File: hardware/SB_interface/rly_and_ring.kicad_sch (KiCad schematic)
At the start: 12 parts, among them K2 J104D2C12VDC.36S, Q3 2N7002

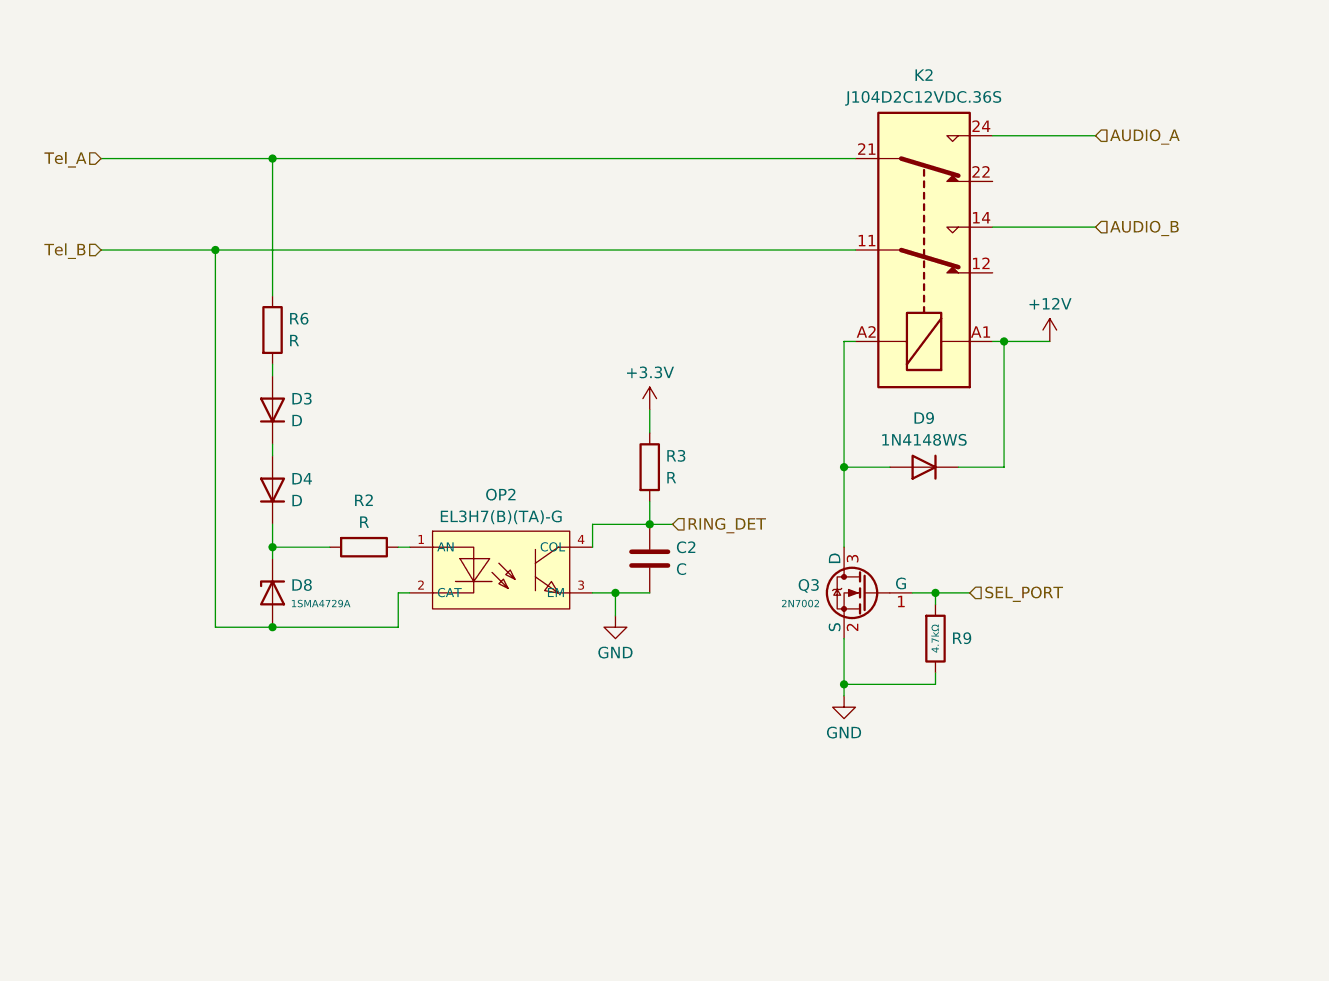
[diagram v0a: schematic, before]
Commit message: current source for ring det. + main 8p8c pinout corrected
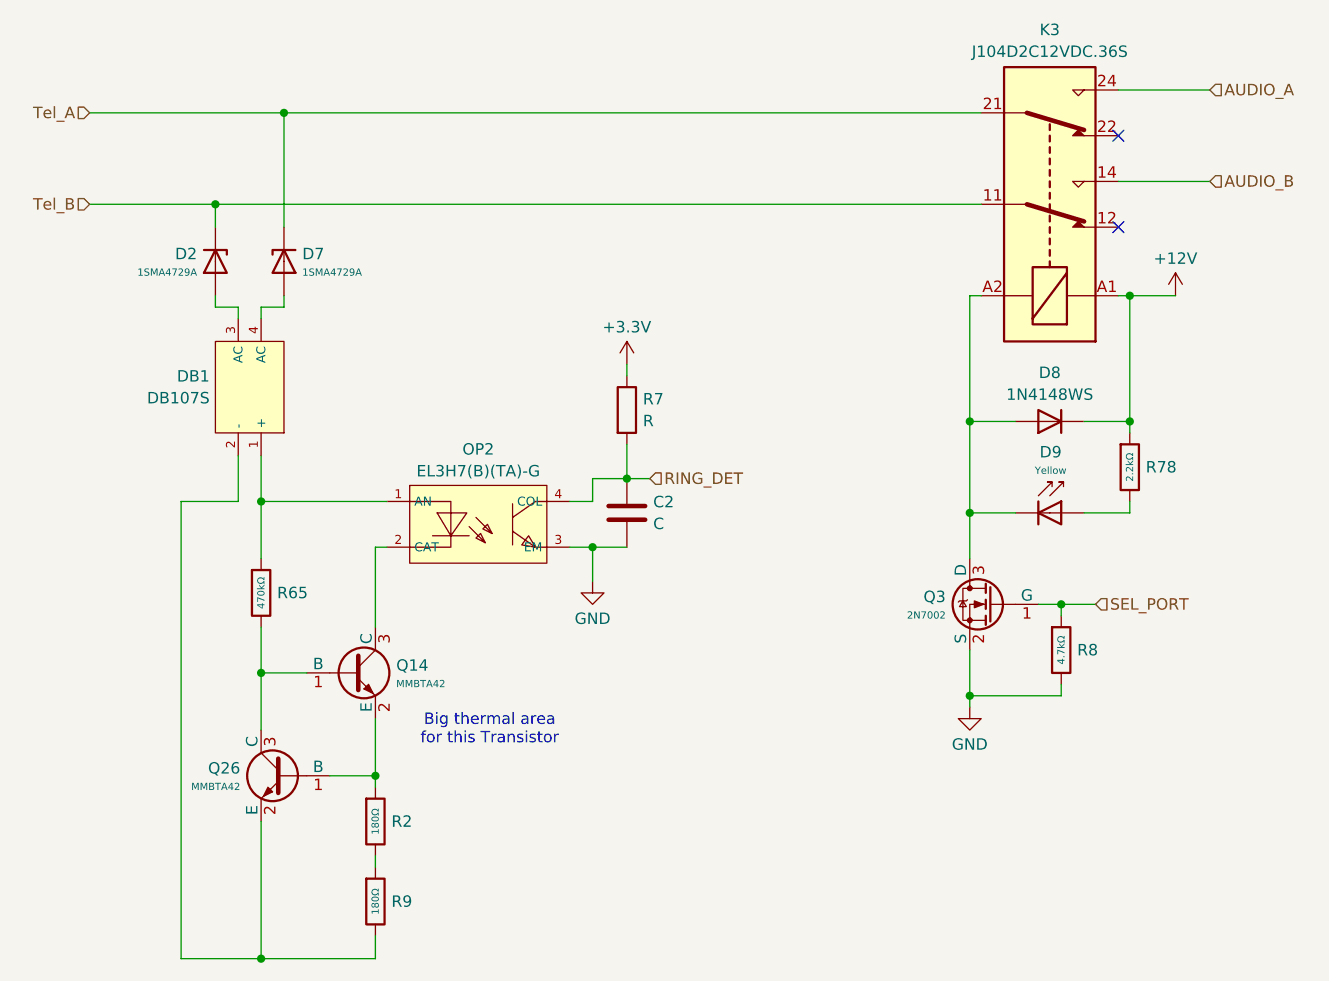
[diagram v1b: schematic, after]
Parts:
- removed D3, D4: D, symbol Device:D
- removed R2, R6: R, symbol Device:R
- added D2: 1SMA4729A, PCM_JLCPCB:D_SMA, symbol PCM_JLCPCB-Diodes:Zener,1SMA4729A
- added D9: Yellow, PCM_JLCPCB:D_0805, symbol PCM_JLCPCB-Diodes:LED,0805,Yellow
- added DB1: DB107S, PCM_JLCPCB:DBS_L8.2-W6.4-P5.10-LS10.0-BL, symbol PCM_JLCPCB-Diode-Packages:Bridge Rectifier, DB107S
- added Q14, Q26: MMBTA42, PCM_JLCPCB:Q_SOT-23, symbol PCM_JLCPCB-Transistors:NPN,MMBTA42
- added R2, R9: 180Ω, PCM_JLCPCB:R_2010, symbol PCM_JLCPCB-Resistors:2010,180Ω
- added R65: 470kΩ, PCM_JLCPCB:R_0805, symbol PCM_JLCPCB-Resistors:0805,470kΩ
- added R78: 2.2kΩ, PCM_JLCPCB:R_0805, symbol PCM_JLCPCB-Resistors:0805,2.2kΩ
- renumbered D8 to D7, D9 to D8, K2 to K3, R3 to R7, R9 to R8
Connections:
- net +12V: now also R78.1
- net Tel_A: now also D7.1
- net Tel_B: now also D2.1; no longer D7.2, OP2.2 (CAT)
- net at D8.2 (A), K3.A2, Q3.3 (D): now also D9.1
- net at OP2.1 (AN): now also DB1.1 (+), R65.1
- new net: Q14.2 (E), Q26.1 (B), R2.1
- new net: R2.2, R9.1
- new net: DB1.2 (-), Q26.2 (E), R9.2
- new net: Q14.1 (B), Q26.3 (C), R65.2
- new net: D2.2, DB1.3 (AC)
- new net: D9.2, R78.2
- new net: OP2.2 (CAT), Q14.3 (C)
- new net: D7.2, DB1.4 (AC)
- no-connect marks 0 -> 2
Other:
- note added: "Big thermal area for this Transistor"
- moved on the sheet: C2, D7, D8, K3, OP2, Q3, R7, R8

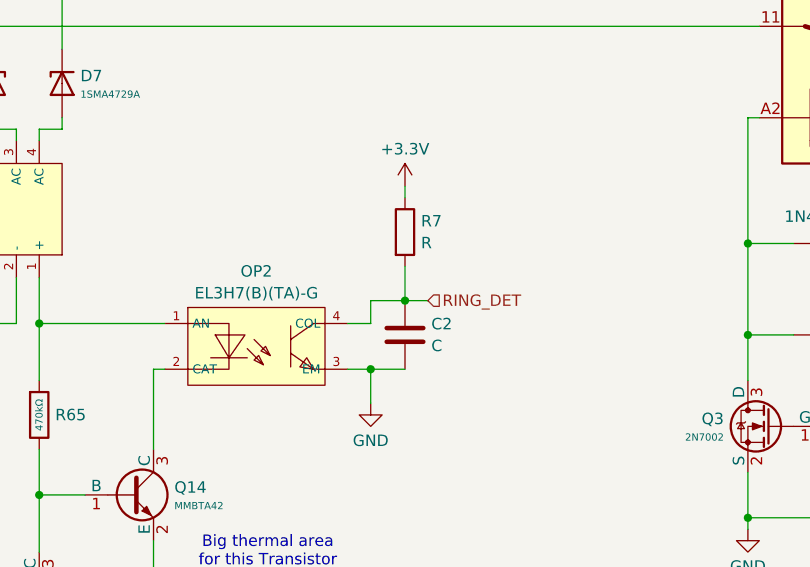
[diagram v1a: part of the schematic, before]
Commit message: assigneld footprints + started layout
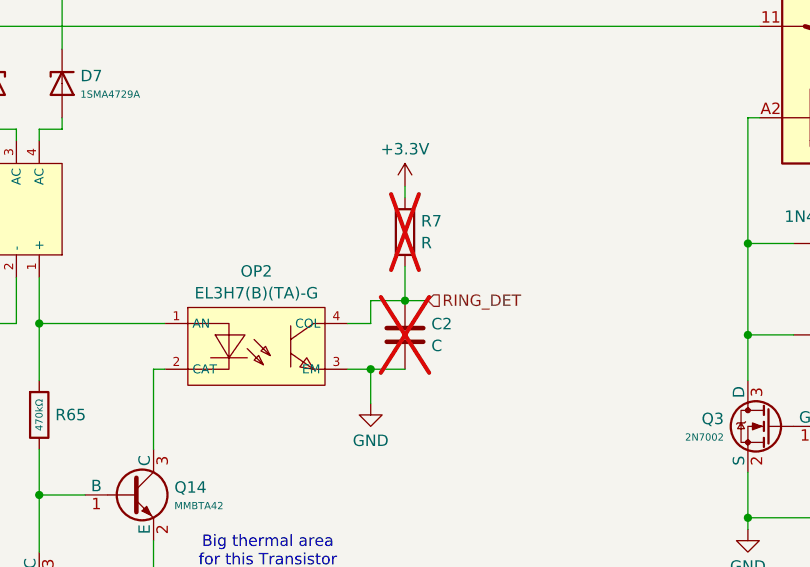
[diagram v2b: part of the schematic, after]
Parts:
- C2: footprint (none) -> Capacitor_SMD:C_0805_2012Metric_Pad1.18x1.45mm_HandSolder; now not fitted
- K3: footprint (none) -> sb_interface:J104D2C12VDC.36S
- R7: footprint (none) -> Resistor_SMD:R_0805_2012Metric_Pad1.20x1.40mm_HandSolder; now not fitted
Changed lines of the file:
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@@
 		(in_bom yes)
 		(on_board yes)
-		(dnp no)
+		(dnp yes)
 		(fields_autoplaced yes)
 		(property "Reference" "C2"
@@
 			)
 		)
-		(property "Footprint" ""
+		(property "Footprint" "Capacitor_SMD:C_0805_2012Metric_Pad1.18x1.45mm_HandSolder"
 			(at 84.7852 76.2 0)
 			(effects
@@
 		(in_bom yes)
 		(on_board yes)
-		(dnp no)
+		(dnp yes)
 		(fields_autoplaced yes)
 		(property "Reference" "R7"
@@
 			)
 		)
-		(property "Footprint" ""
+		(property "Footprint" "Resistor_SMD:R_0805_2012Metric_Pad1.20x1.40mm_HandSolder"
 			(at 82.042 60.96 90)
 			(effects
@@
 			)
 		)
-		(property "Footprint" ""
+		(property "Footprint" "sb_interface:J104D2C12VDC.36S"
 			(at 129.54 21.59 0)
 			(effects

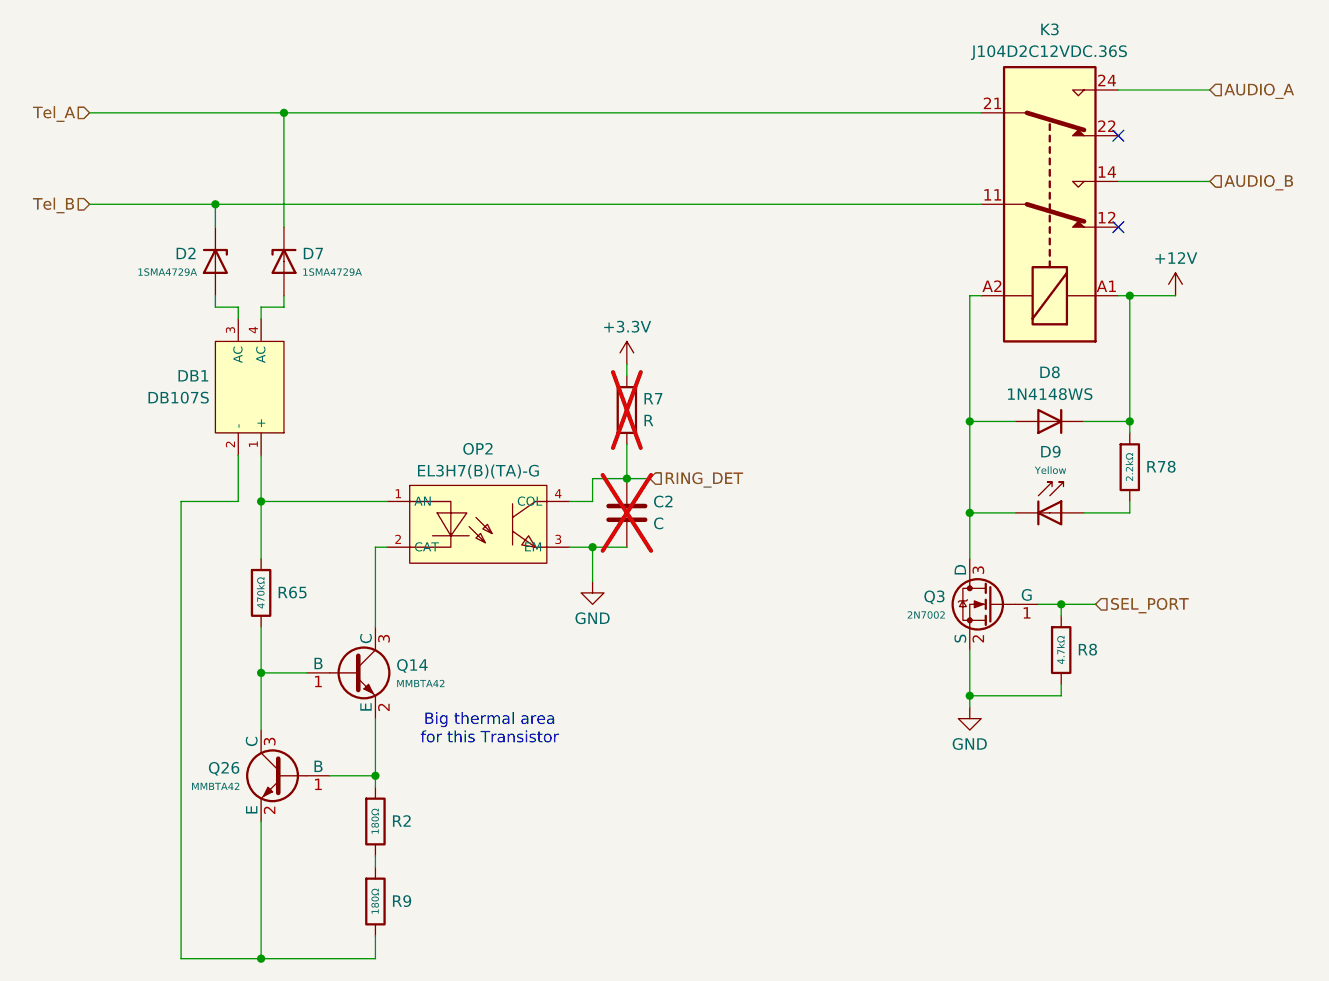
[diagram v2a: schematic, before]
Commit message: replicated layout + added JLCPCB Design rules file
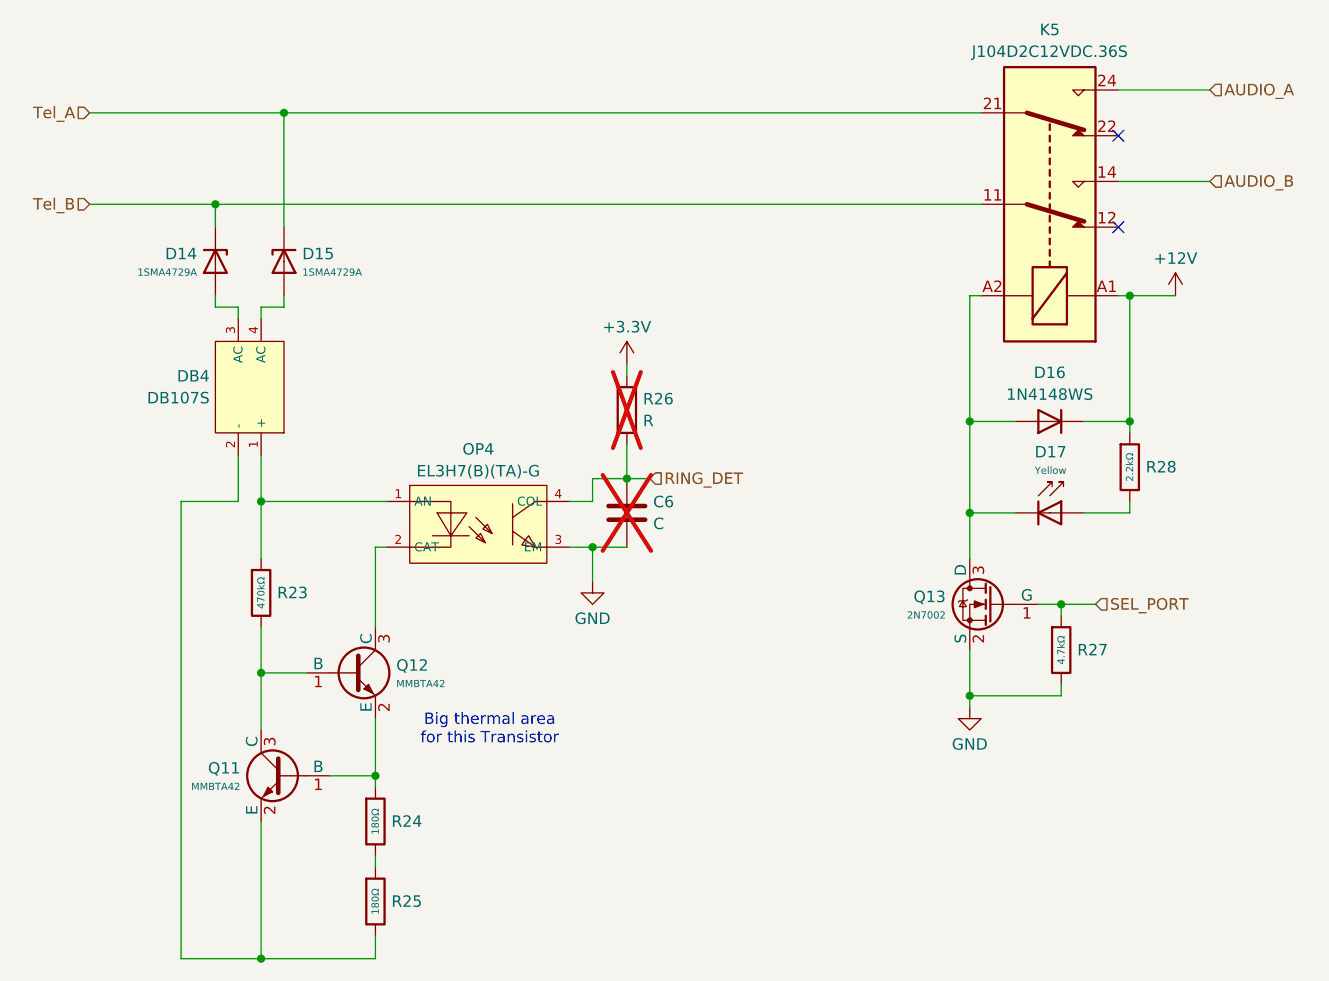
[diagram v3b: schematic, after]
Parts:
- D17: renamed from D9; Stock 385221 -> 454868
- DB4: renamed from DB1; Stock 116898 -> 115385
- OP4: renamed from OP2; Stock 516875 -> 505293
- Q11: renamed from Q26; Stock 65595 -> 65571
- Q12: renamed from Q14; Stock 65595 -> 65571
- Q13: renamed from Q3; Stock 572214 -> 926097
- R23: renamed from R65; Stock 596116 -> 589101
- R24: renamed from R2; Stock 21780 -> 20280
- R25: renamed from R9; Stock 21780 -> 20280
- R27: renamed from R8; Stock 2133514 -> 2078920
- R28: renamed from R78; Stock 1558470 -> 1555719
- renumbered C2 to C6, D2 to D14, D7 to D15, D8 to D16, K3 to K5, R7 to R26

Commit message: layout of tel inputs
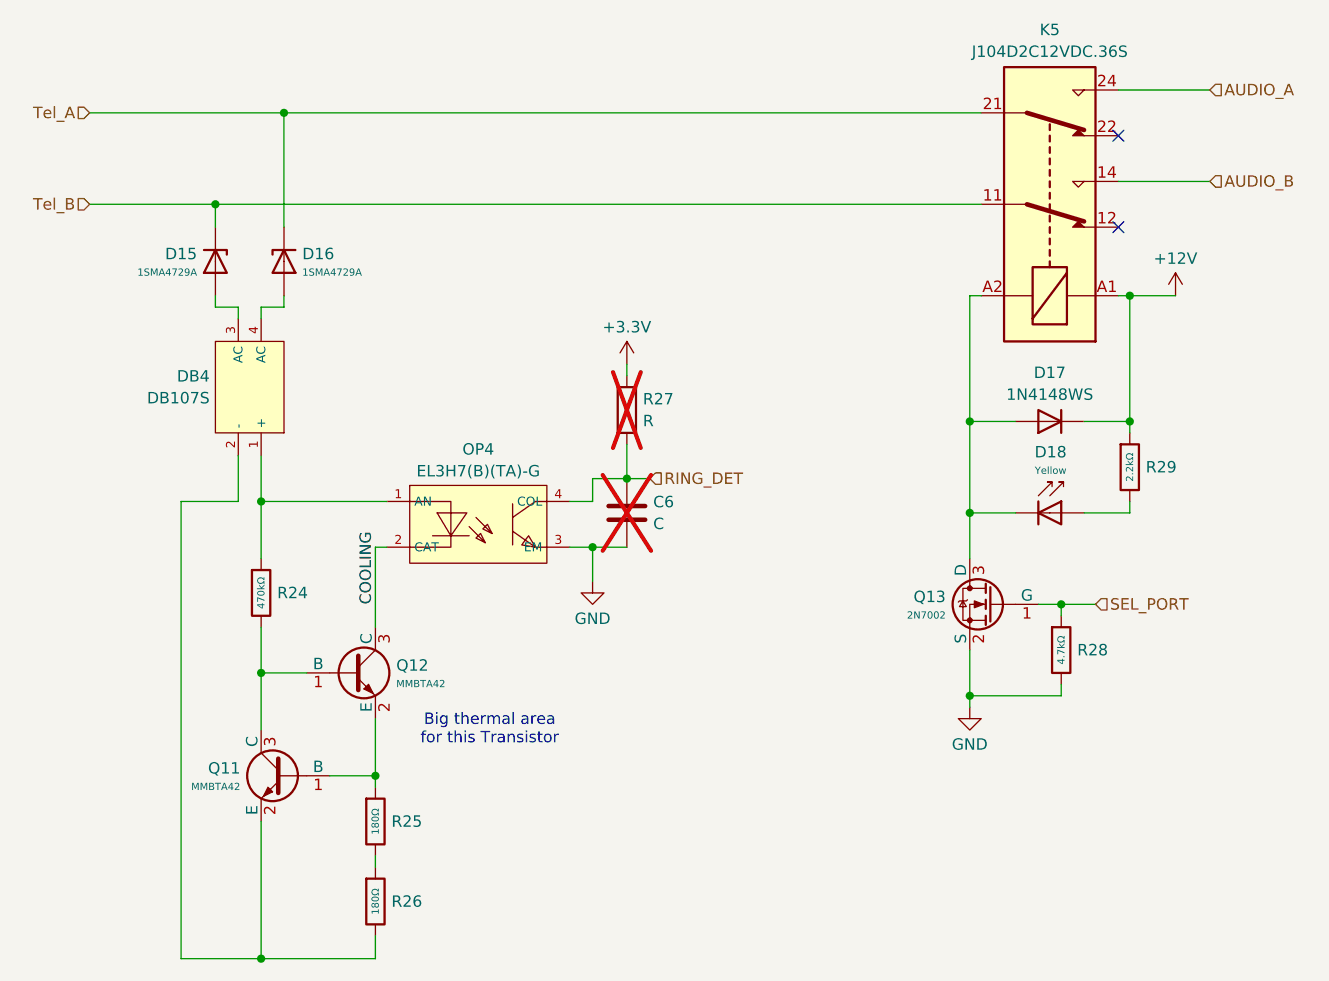
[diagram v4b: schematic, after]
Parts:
- renumbered D14 to D15, D15 to D16, D16 to D17, D17 to D18, R23 to R24, R24 to R25, R25 to R26, R26 to R27, R27 to R28, R28 to R29
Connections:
- net COOLING: now reaches OP4.2 (CAT), Q12.3 (C)
